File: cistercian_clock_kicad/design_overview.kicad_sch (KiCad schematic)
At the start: 121 parts

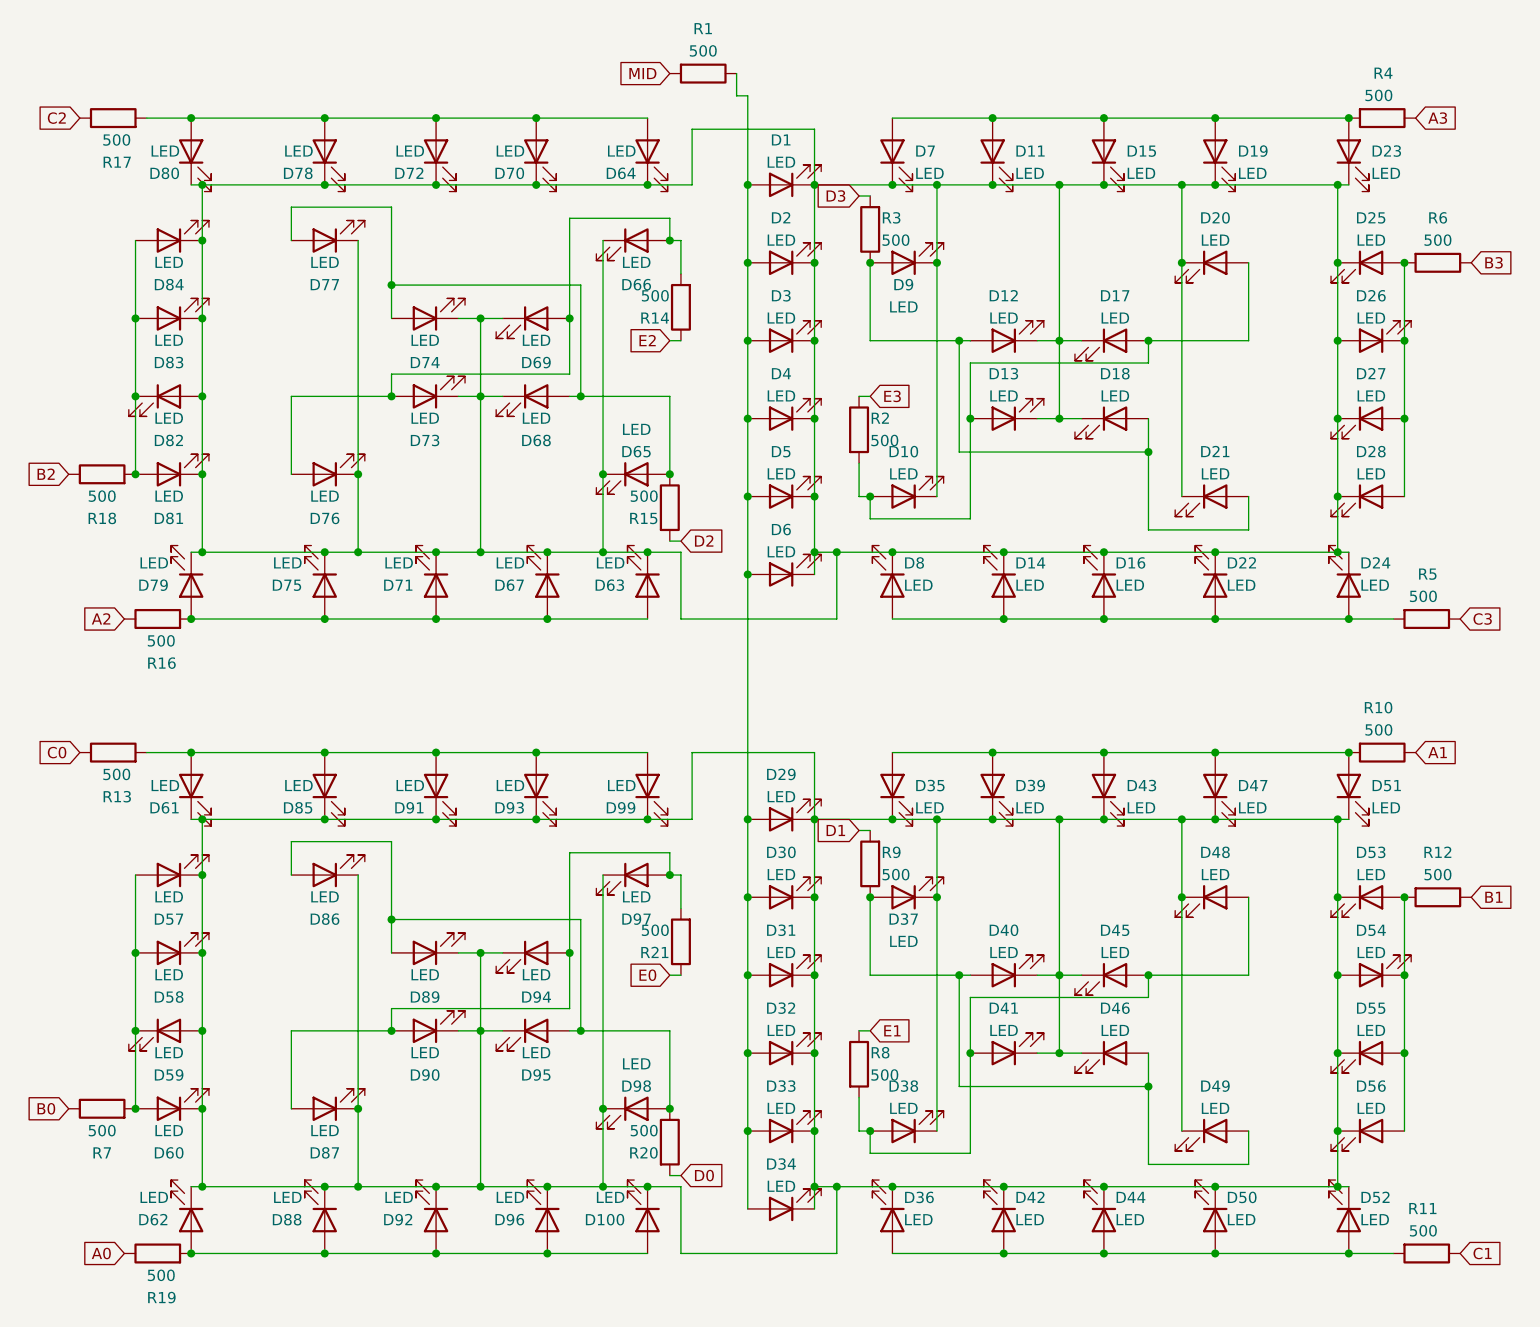
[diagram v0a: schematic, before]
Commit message: started code for clock cycles, updated schematics
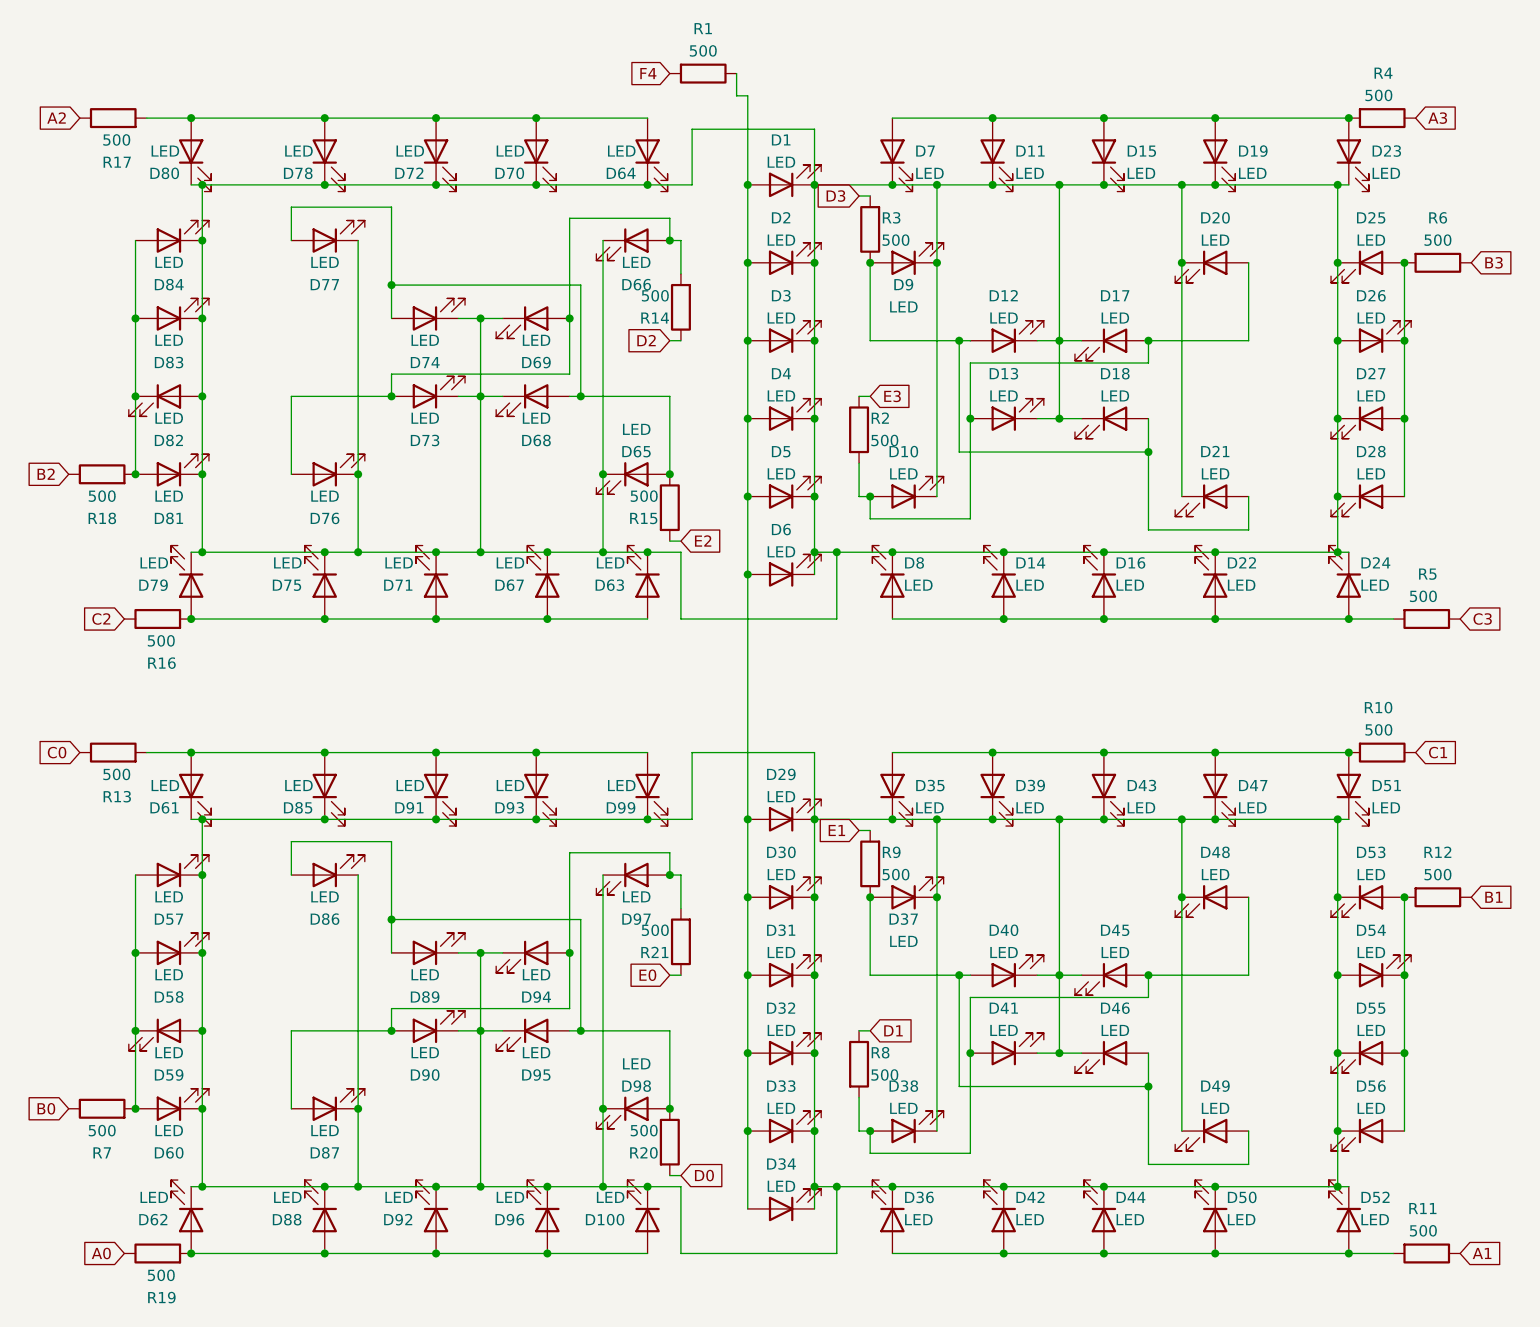
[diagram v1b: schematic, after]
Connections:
- net A1: now also R11.1; no longer R10.1
- net A2: now also R17.1; no longer R16.1
- net C1: now also R10.1; no longer R11.1
- net C2: now also R16.1; no longer R17.1
- net D1: now also R8.1; no longer R9.2
- net D2: now also R14.1; no longer R15.2
- net E1: now also R9.2; no longer R8.1
- net E2: now also R15.2; no longer R14.1
- net MID renamed F4
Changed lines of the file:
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@@
     )
   )
-  (global_label "MID" (shape input) (at 149.86 19.05 180) (fields_autoplaced)
+  (global_label "F4" (shape input) (at 149.86 19.05 180) (fields_autoplaced)
     (effects (font (size 1.27 1.27)) (justify right))
-    (property "Intersheetrefs" "${INTERSHEET_REFS}" (at 143.5486 19.05 0)
+    (property "Intersheetrefs" "${INTERSHEET_REFS}" (at 144.5767 19.05 0)
       (effects (font (size 1.27 1.27)) (justify right) hide)
     )
@@
     )
   )
-  (global_label "C1" (shape input) (at 240.03 153.67 0) (fields_autoplaced)
-    (effects (font (size 1.27 1.27)) (justify left))
-    (property "Intersheetrefs" "${INTERSHEET_REFS}" (at 245.4947 153.67 0)
-      (effects (font (size 1.27 1.27)) (justify left) hide)
-    )
-  )
   (global_label "B0" (shape input) (at 81.28 137.16 180) (fields_autoplaced)
     (effects (font (size 1.27 1.27)) (justify right))
     (property "Intersheetrefs" "${INTERSHEET_REFS}" (at 75.8153 137.16 0)
+      (effects (font (size 1.27 1.27)) (justify right) hide)
+    )
+  )
+  (global_label "A2" (shape input) (at 82.55 24.13 180) (fields_autoplaced)
+    (effects (font (size 1.27 1.27)) (justify right))
+    (property "Intersheetrefs" "${INTERSHEET_REFS}" (at 77.2667 24.13 0)
       (effects (font (size 1.27 1.27)) (justify right) hide)
     )
@@
     )
   )
-  (global_label "D2" (shape input) (at 151.13 72.39 0) (fields_autoplaced)
+  (global_label "E2" (shape input) (at 151.13 72.39 0) (fields_autoplaced)
     (effects (font (size 1.27 1.27)) (justify left))
-    (property "Intersheetrefs" "${INTERSHEET_REFS}" (at 156.5947 72.39 0)
+    (property "Intersheetrefs" "${INTERSHEET_REFS}" (at 156.4737 72.39 0)
       (effects (font (size 1.27 1.27)) (justify left) hide)
     )
@@
     )
   )
-  (global_label "E2" (shape input) (at 149.86 49.53 180) (fields_autoplaced)
-    (effects (font (size 1.27 1.27)) (justify right))
-    (property "Intersheetrefs" "${INTERSHEET_REFS}" (at 144.5163 49.53 0)
-      (effects (font (size 1.27 1.27)) (justify right) hide)
-    )
-  )
-  (global_label "E1" (shape input) (at 172.72 128.27 0) (fields_autoplaced)
+  (global_label "C1" (shape input) (at 234.95 96.52 0) (fields_autoplaced)
     (effects (font (size 1.27 1.27)) (justify left))
-    (property "Intersheetrefs" "${INTERSHEET_REFS}" (at 178.0637 128.27 0)
+    (property "Intersheetrefs" "${INTERSHEET_REFS}" (at 240.4147 96.52 0)
       (effects (font (size 1.27 1.27)) (justify left) hide)
     )
@@
     )
   )
-  (global_label "D1" (shape input) (at 171.45 105.41 180) (fields_autoplaced)
-    (effects (font (size 1.27 1.27)) (justify right))
-    (property "Intersheetrefs" "${INTERSHEET_REFS}" (at 165.9853 105.41 0)
-      (effects (font (size 1.27 1.27)) (justify right) hide)
-    )
-  )
-  (global_label "C2" (shape input) (at 82.55 24.13 180) (fields_autoplaced)
-    (effects (font (size 1.27 1.27)) (justify right))
-    (property "Intersheetrefs" "${INTERSHEET_REFS}" (at 77.0853 24.13 0)
-      (effects (font (size 1.27 1.27)) (justify right) hide)
-    )
-  )
-  (global_label "A1" (shape input) (at 234.95 96.52 0) (fields_autoplaced)
-    (effects (font (size 1.27 1.27)) (justify left))
-    (property "Intersheetrefs" "${INTERSHEET_REFS}" (at 240.2333 96.52 0)
-      (effects (font (size 1.27 1.27)) (justify left) hide)
-    )
-  )
   (global_label "E0" (shape input) (at 149.86 121.92 180) (fields_autoplaced)
     (effects (font (size 1.27 1.27)) (justify right))
@@
     )
   )
-  (global_label "A2" (shape input) (at 87.63 81.28 180) (fields_autoplaced)
+  (global_label "D1" (shape input) (at 172.72 128.27 0) (fields_autoplaced)
+    (effects (font (size 1.27 1.27)) (justify left))
+    (property "Intersheetrefs" "${INTERSHEET_REFS}" (at 178.1847 128.27 0)
+      (effects (font (size 1.27 1.27)) (justify left) hide)
+    )
+  )
+  (global_label "A1" (shape input) (at 240.03 153.67 0) (fields_autoplaced)
+    (effects (font (size 1.27 1.27)) (justify left))
+    (property "Intersheetrefs" "${INTERSHEET_REFS}" (at 245.3133 153.67 0)
+      (effects (font (size 1.27 1.27)) (justify left) hide)
+    )
+  )
+  (global_label "E1" (shape input) (at 171.45 105.41 180) (fields_autoplaced)
     (effects (font (size 1.27 1.27)) (justify right))
-    (property "Intersheetrefs" "${INTERSHEET_REFS}" (at 82.3467 81.28 0)
+    (property "Intersheetrefs" "${INTERSHEET_REFS}" (at 166.1063 105.41 0)
       (effects (font (size 1.27 1.27)) (justify right) hide)
     )
@@
     (effects (font (size 1.27 1.27)) (justify right))
     (property "Intersheetrefs" "${INTERSHEET_REFS}" (at 75.8153 64.77 0)
+      (effects (font (size 1.27 1.27)) (justify right) hide)
+    )
+  )
+  (global_label "C2" (shape input) (at 87.63 81.28 180) (fields_autoplaced)
+    (effects (font (size 1.27 1.27)) (justify right))
+    (property "Intersheetrefs" "${INTERSHEET_REFS}" (at 82.1653 81.28 0)
       (effects (font (size 1.27 1.27)) (justify right) hide)
     )
@@
     )
   )
+  (global_label "D2" (shape input) (at 149.86 49.53 180) (fields_autoplaced)
+    (effects (font (size 1.27 1.27)) (justify right))
+    (property "Intersheetrefs" "${INTERSHEET_REFS}" (at 144.3953 49.53 0)
+      (effects (font (size 1.27 1.27)) (justify right) hide)
+    )
+  )
